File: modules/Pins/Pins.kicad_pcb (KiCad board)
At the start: 2 copper layers, 40.6 x 40.6 mm, 37 parts, among them J1 2, J10 11, J11 12, J12 13, J13 A0, J14 A1, J15 A2, J16 A3, J17 A4, J18 A5, J19 Vcc, J2 3, J20 Gnd, J21 Conn_01x12_Male, J22 Conn_01x12_Male, J23 Conn_01x12_Male, J24 Conn_01x06_Male, J25 Conn_01x06_Male, J26 Conn_01x06_Male, J27 Conn_01x04_Male, J28 Conn_01x04_Male, J29 Conn_01x04_Male, J3 4, J30 Conn_01x06_Male, J31 Conn_01x06_Male, J4 5, J5 6, J6 7, J7 8, J8 9, J9 10

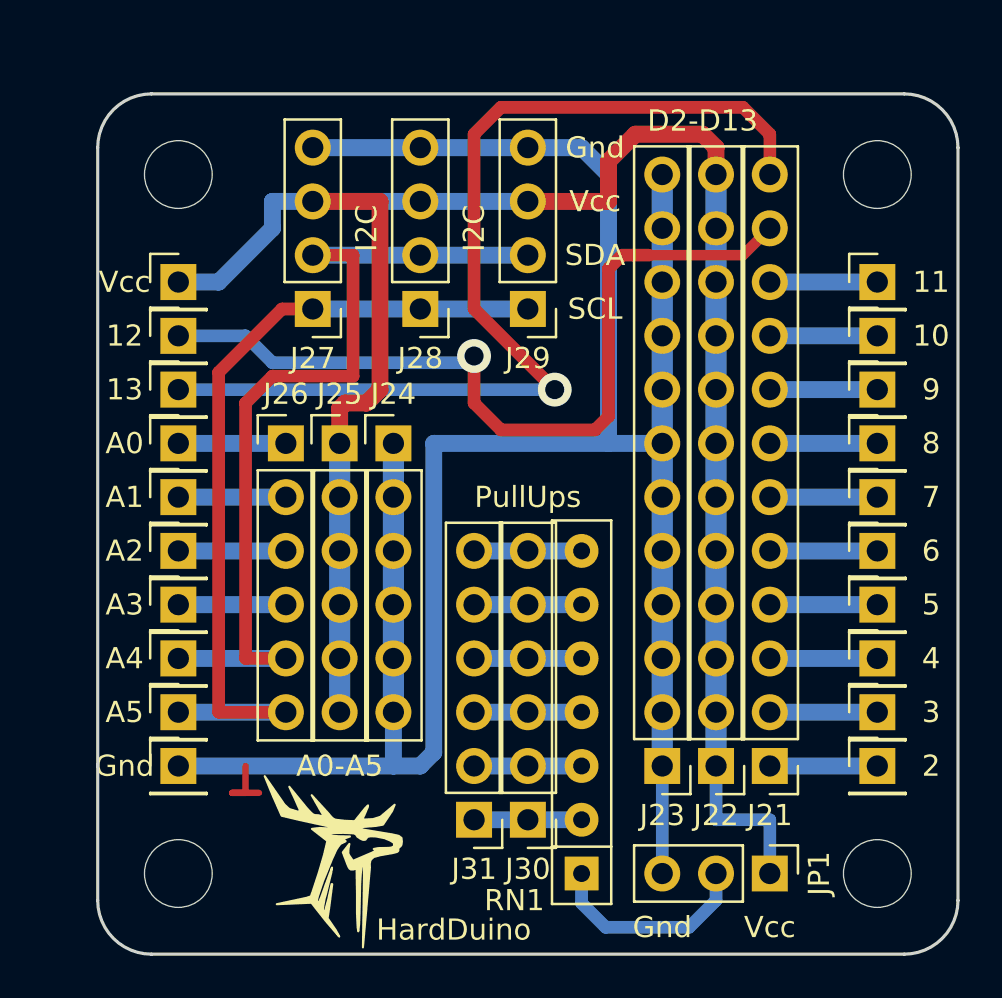
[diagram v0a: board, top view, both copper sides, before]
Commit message: Lost labels
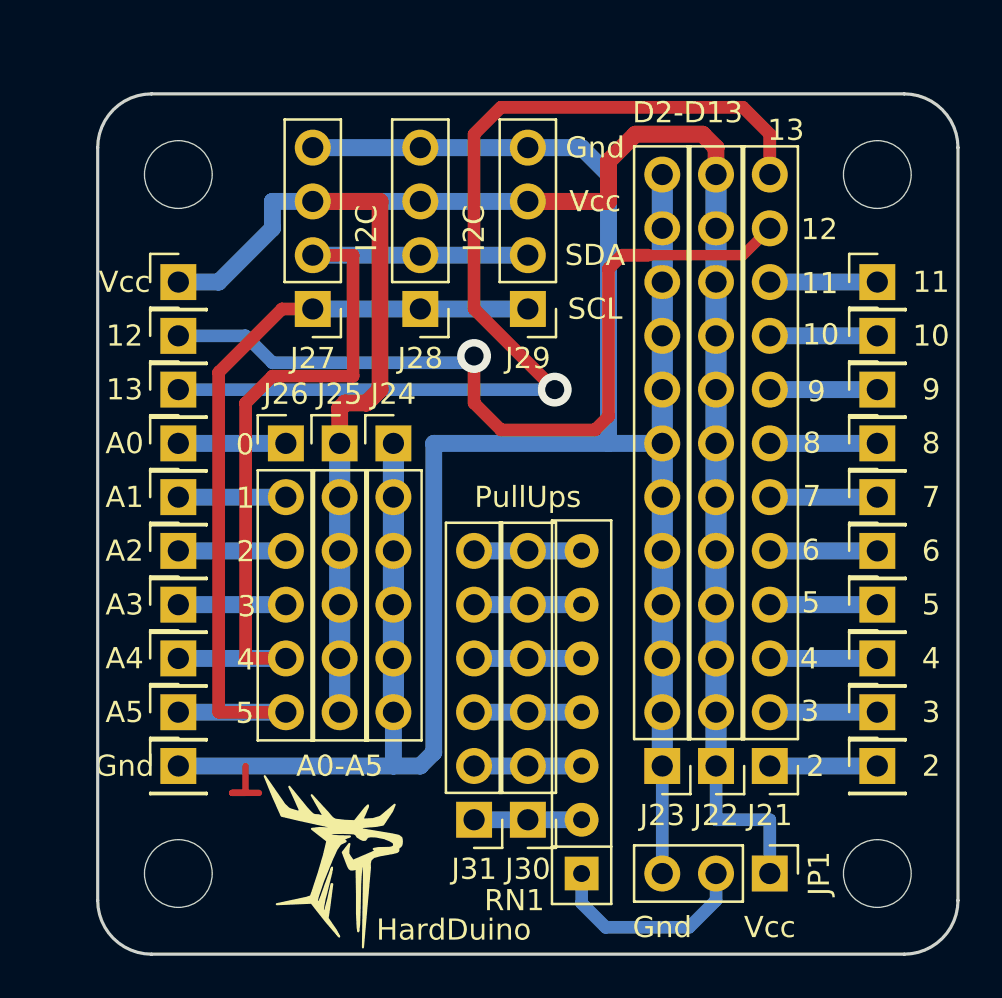
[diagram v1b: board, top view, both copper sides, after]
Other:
- board text added: "0"
- board text added: "1"
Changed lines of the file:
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@@
   (general
     (thickness 1.6)
-    (drawings 41)
+    (drawings 59)
     (tracks 102)
     (zones 0)
@@
       (outputformat 1)
       (mirror false)
-      (drillshape 1)
+      (drillshape 0)
       (scaleselection 1)
-      (outputdirectory ""))
+      (outputdirectory "pins/"))
   )
   (net 0 "")
@@
     )
   )
+  (gr_text 2 (at 122.8 82.56) (layer F.SilkS)
+    (effects (font (size 1 1) (thickness 0.15)))
+  )
+  (gr_text 3 (at 122.55 79.96) (layer F.SilkS)
+    (effects (font (size 1 1) (thickness 0.15)))
+  )
+  (gr_text 4 (at 122.51 77.48) (layer F.SilkS)
+    (effects (font (size 1 1) (thickness 0.15)))
+  )
+  (gr_text 5 (at 122.59 74.83) (layer F.SilkS)
+    (effects (font (size 1 1) (thickness 0.15)))
+  )
+  (gr_text 6 (at 122.59 72.35) (layer F.SilkS)
+    (effects (font (size 1 1) (thickness 0.15)))
+  )
+  (gr_text 7 (at 122.64 69.81) (layer F.SilkS)
+    (effects (font (size 1 1) (thickness 0.15)))
+  )
+  (gr_text 8 (at 122.64 67.29) (layer F.SilkS)
+    (effects (font (size 1 1) (thickness 0.15)))
+  )
+  (gr_text 9 (at 122.85 64.86) (layer F.SilkS)
+    (effects (font (size 1 1) (thickness 0.15)))
+  )
+  (gr_text 10 (at 123.06 62.17) (layer F.SilkS)
+    (effects (font (size 1 1) (thickness 0.15)))
+  )
+  (gr_text 11 (at 123.01 59.75) (layer F.SilkS)
+    (effects (font (size 1 1) (thickness 0.15)))
+  )
+  (gr_text 12 (at 122.99 57.2) (layer F.SilkS)
+    (effects (font (size 1 1) (thickness 0.15)))
+  )
+  (gr_text 13 (at 121.41 52.51) (layer F.SilkS)
+    (effects (font (size 1 1) (thickness 0.15)))
+  )
+  (gr_text 5 (at 95.85 80.05) (layer F.SilkS)
+    (effects (font (size 1 1) (thickness 0.15)))
+  )
+  (gr_text 4 (at 95.89 77.53) (layer F.SilkS)
+    (effects (font (size 1 1) (thickness 0.15)))
+  )
+  (gr_text 3 (at 95.95 75.01) (layer F.SilkS)
+    (effects (font (size 1 1) (thickness 0.15)))
+  )
+  (gr_text 2 (at 95.89 72.42) (layer F.SilkS)
+    (effects (font (size 1 1) (thickness 0.15)))
+  )
+  (gr_text 1 (at 95.88 69.89) (layer F.SilkS)
+    (effects (font (size 1 1) (thickness 0.15)))
+  )
+  (gr_text 0 (at 95.86 67.37) (layer F.SilkS)
+    (effects (font (size 1 1) (thickness 0.15)))
+  )
   (gr_text Vcc (at 112.395 55.88) (layer F.SilkS)
     (effects (font (size 1 1) (thickness 0.15)))
@@
     (effects (font (size 1 1) (thickness 0.15)))
   )
-  (gr_text D2-D13 (at 117.475 52.07) (layer F.SilkS)
-    (effects (font (size 1 1) (thickness 0.15)))
-  )
+  (gr_text D2-D13 (at 116.77 51.68) (layer F.SilkS)
+    (effects (font (size 1 1) (thickness 0.15)))
+  )

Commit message: 1x PCBs. Move holes to edges. Caution! This changes is uncompatible with previous versions...
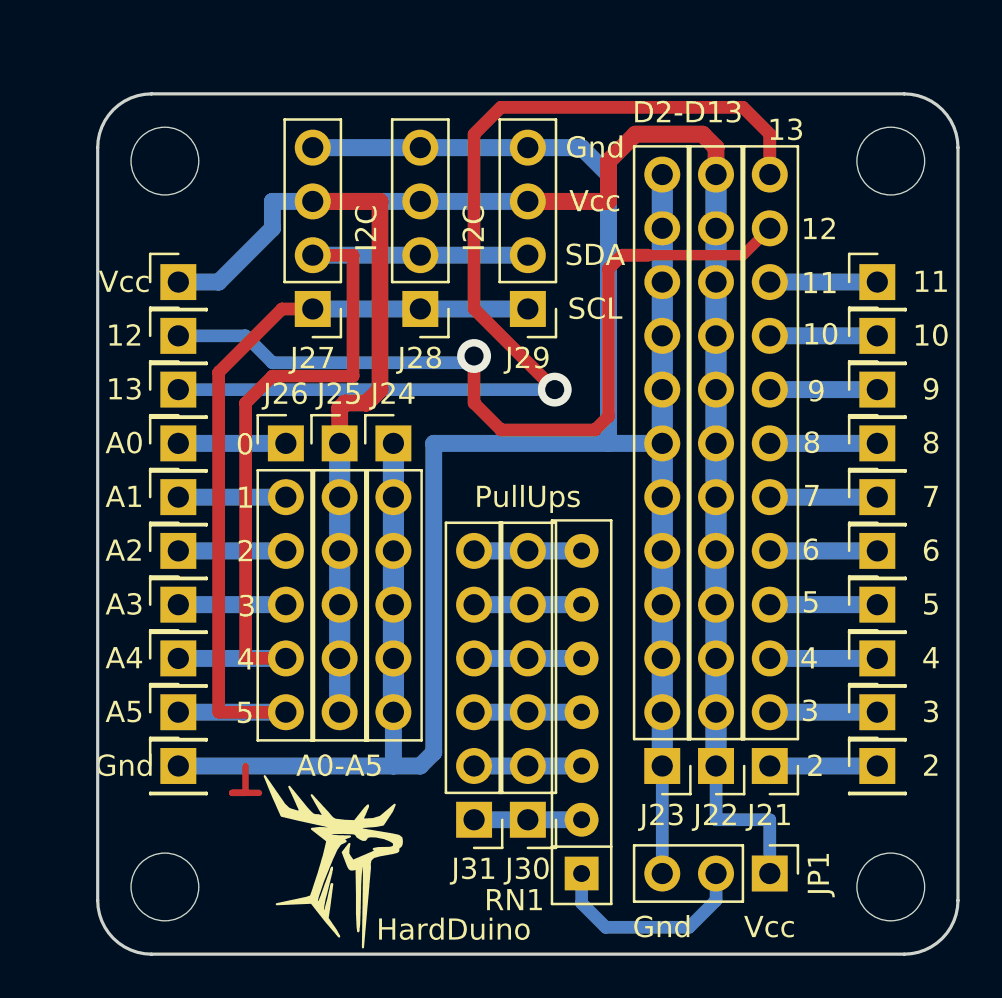
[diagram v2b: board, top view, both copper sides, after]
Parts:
- moved H2 0.90 mm to (92.1, 88.3)
- moved H4 0.90 mm to (126.4, 88.3)
- moved H1 0.90 mm to (92.1, 54.0)
- moved H3 0.90 mm to (126.4, 54.0)
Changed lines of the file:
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@@
   )
   (module MountingHole:MountingHole_3.2mm_M3 (layer F.Cu)
-    (at 92.71 54.61)
+    (at 92.0750 53.9750)
     (descr "Mounting Hole 3.2mm, no annular, M3")
     (tags "mounting hole 3.2mm no annular m3")
@@
   )
   (module MountingHole:MountingHole_3.2mm_M3 (layer F.Cu)
-    (at 92.71 87.63)
+    (at 92.0750 88.2650)
     (descr "Mounting Hole 3.2mm, no annular, M3")
     (tags "mounting hole 3.2mm no annular m3")
@@
   )
   (module MountingHole:MountingHole_3.2mm_M3 (layer F.Cu)
-    (at 125.73 54.61)
+    (at 126.3650 53.9750)
     (descr "Mounting Hole 3.2mm, no annular, M3")
     (tags "mounting hole 3.2mm no annular m3")
@@
   )
   (module MountingHole:MountingHole_3.2mm_M3 (layer F.Cu)
-    (at 125.73 87.63)
+    (at 126.3650 88.2650)
     (descr "Mounting Hole 3.2mm, no annular, M3")
     (tags "mounting hole 3.2mm no annular m3")

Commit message: Fix hash & version
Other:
- board text added: "21.02.2021"
- board text added: "b4d799"
- board text added: "v2.3"

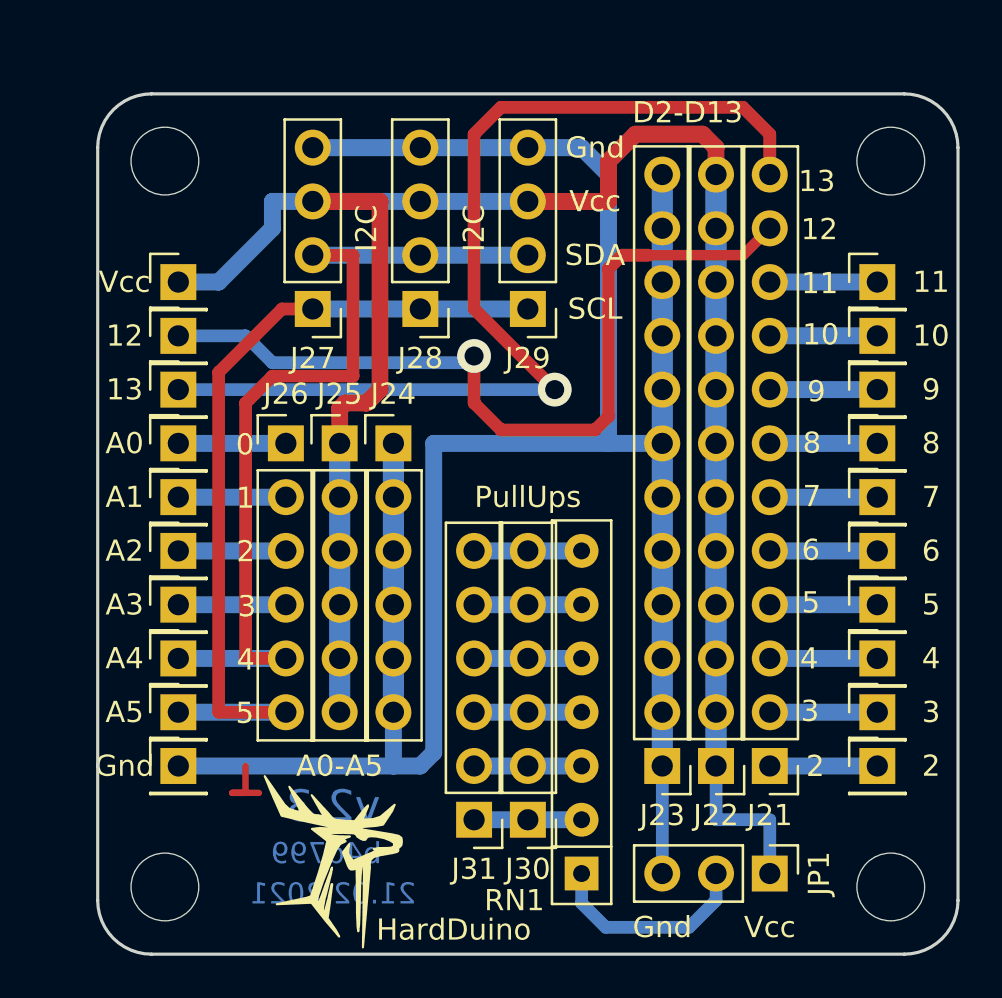
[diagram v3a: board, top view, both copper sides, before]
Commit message: All 1x shields was rotated clockwise
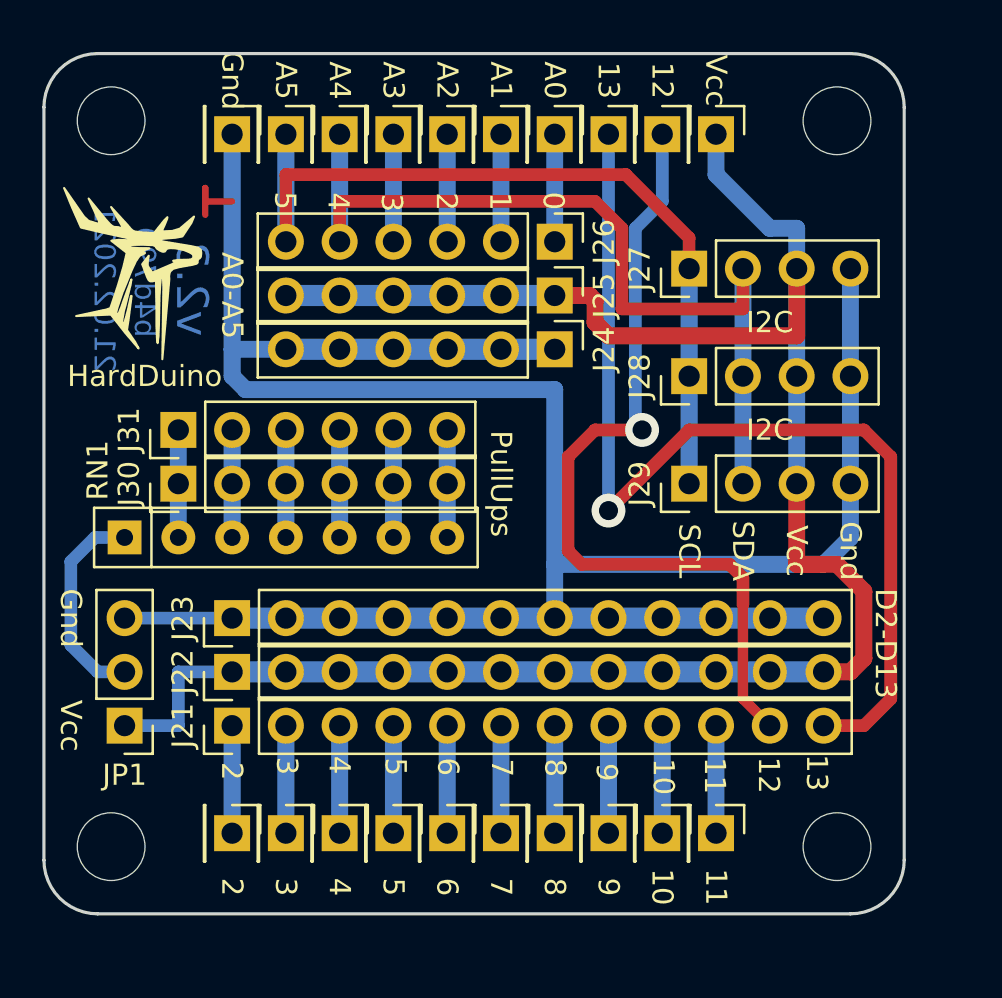
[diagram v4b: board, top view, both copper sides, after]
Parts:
- moved H4 36.9 mm to (89.5, 86.4), turned to 270 degrees
- moved H2 36.3 mm to (89.5, 52.1), turned to 270 degrees
- moved H3 32.5 mm to (123.8, 86.4), turned to 270 degrees
- moved H1 31.8 mm to (123.8, 52.1), turned to 270 degrees
- moved JP1 31.3 mm to (90.2, 80.6), turned to 180 degrees
- moved J1 30.6 mm to (95.2, 85.7), turned to 270 degrees
- moved J20 30.0 mm to (95.2, 52.7), turned to 270 degrees
- moved J2 28.5 mm to (97.8, 85.7), turned to 270 degrees
- moved J18 27.8 mm to (97.8, 52.7), turned to 270 degrees
- moved J10 27.1 mm to (118.1, 85.7), turned to 270 degrees
- moved RN1 26.8 mm to (90.2, 71.8), turned to 0 degrees
- moved J3 26.7 mm to (100.3, 85.7), turned to 270 degrees
- moved J19 26.3 mm to (118.1, 52.7), turned to 270 degrees
- moved J17 25.9 mm to (100.3, 52.7), turned to 270 degrees
- moved J9 25.6 mm to (115.6, 85.7), turned to 270 degrees
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
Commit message: Now all mounting holes have distance 31.92 x 31.1
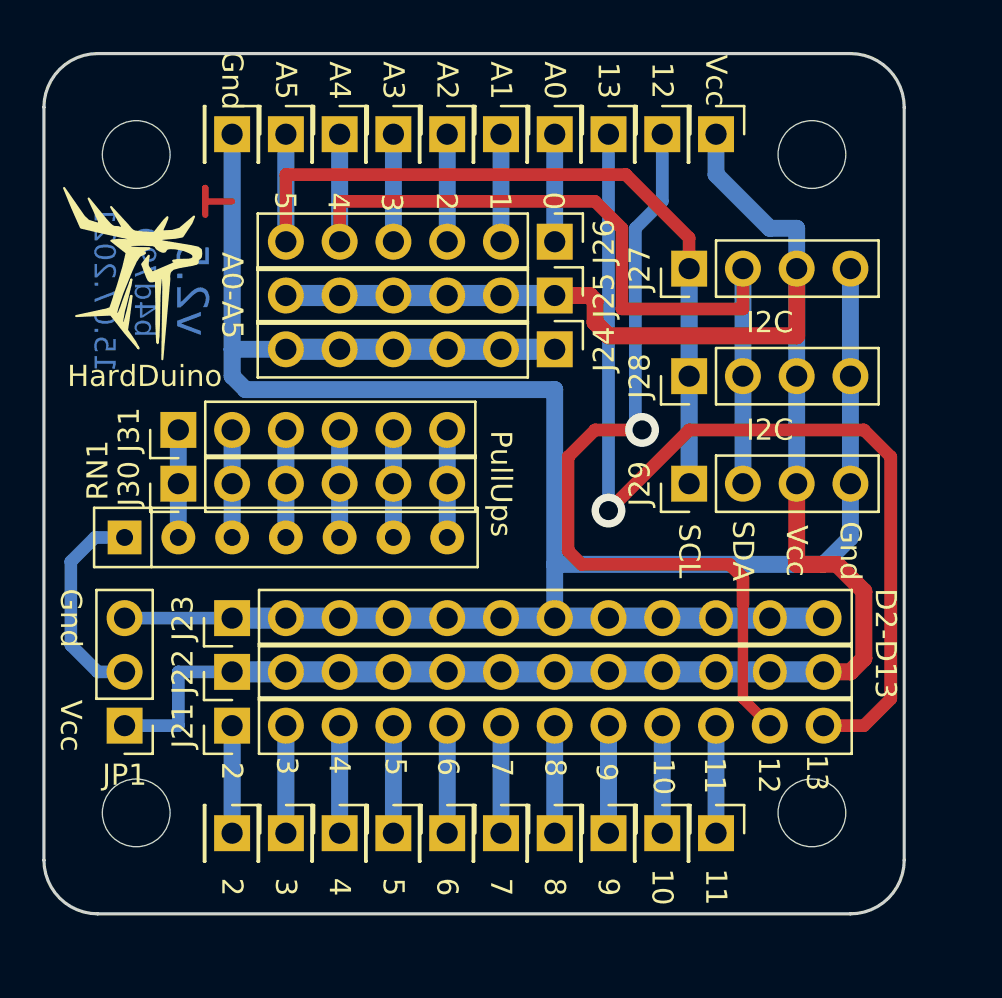
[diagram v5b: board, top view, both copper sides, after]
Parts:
- moved H1 1.99 mm to (122.6, 53.7), turned to 0 degrees
- moved H2 1.99 mm to (90.7, 53.7), turned to 0 degrees
- moved H3 1.99 mm to (122.6, 84.8), turned to 0 degrees
- moved H4 1.99 mm to (90.7, 84.8), turned to 0 degrees
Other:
- board text added: "15.07.2021"
- board text added: "v2.5"
- board text removed: "21.02.2021"
- board text removed: "v2.3"
